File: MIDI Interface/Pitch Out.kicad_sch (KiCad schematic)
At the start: 5 parts, among them J27 AudioJack2_SwitchT, U8 NCS21914

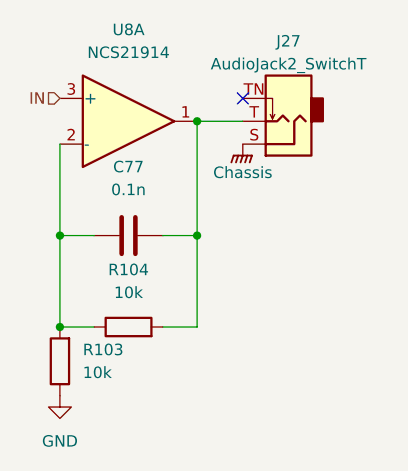
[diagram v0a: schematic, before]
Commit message: Start MIDI interface board
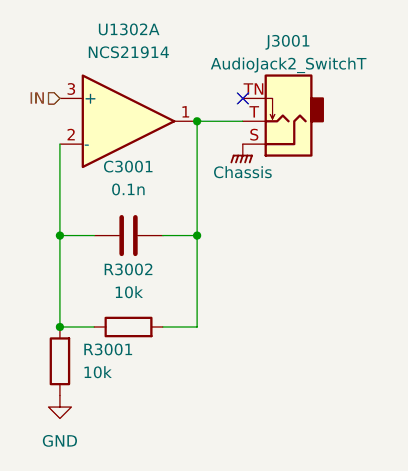
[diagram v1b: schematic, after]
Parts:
- C3001: renamed from C77; footprint (none) -> 0_Capacitor_THT:C_Disc_D5.5mm_W2.5mm_P2.50mm
- J3001: renamed from J27; symbol Connector:AudioJack2_SwitchT -> Connector_Audio:AudioJack2_SwitchT
- R3001: renamed from R103; footprint (none) -> Resistor_THT:R_Axial_DIN0207_L6.3mm_D2.5mm_P7.62mm_Horizontal
- R3002: renamed from R104; footprint (none) -> Resistor_THT:R_Axial_DIN0207_L6.3mm_D2.5mm_P7.62mm_Horizontal
- renumbered U8 to U1302

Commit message: New MIDI controller, new envelope generator
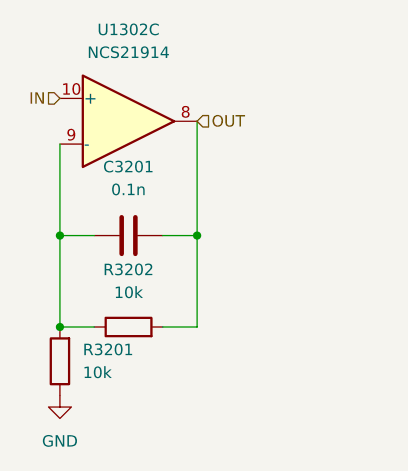
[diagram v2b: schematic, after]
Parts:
- removed J3001: AudioJack2_SwitchT, Connector_Audio:Jack_3.5mm_QingPu_WQP-PJ398SM_Vertical_CircularHoles, symbol Connector_Audio:AudioJack2_SwitchT
- renumbered C3001 to C3201, R3001 to R3201, R3002 to R3202
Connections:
- net IN: now also U1302.10 (+); no longer U1302.3 (+)
- net at C3201.1, R3201.2, R3202.1: now also U1302.9 (-); no longer U1302.2 (-)
- net OUT: now reaches C3201.2, R3202.2
- net OUT: now also U1302.8; no longer U1302.1
- no-connect marks 1 -> 0

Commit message: New VCLPF and Out
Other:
- note added: "0.1% tolerance"
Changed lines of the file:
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@@
+		)
+	)
+	(text "0.1% tolerance"
+		(exclude_from_sim no)
+		(at 149.86 121.666 0)
+		(effects
+			(font
+				(size 1.27 1.27)
+			)
 		)
 	)
